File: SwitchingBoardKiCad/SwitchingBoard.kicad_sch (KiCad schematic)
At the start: 45 parts

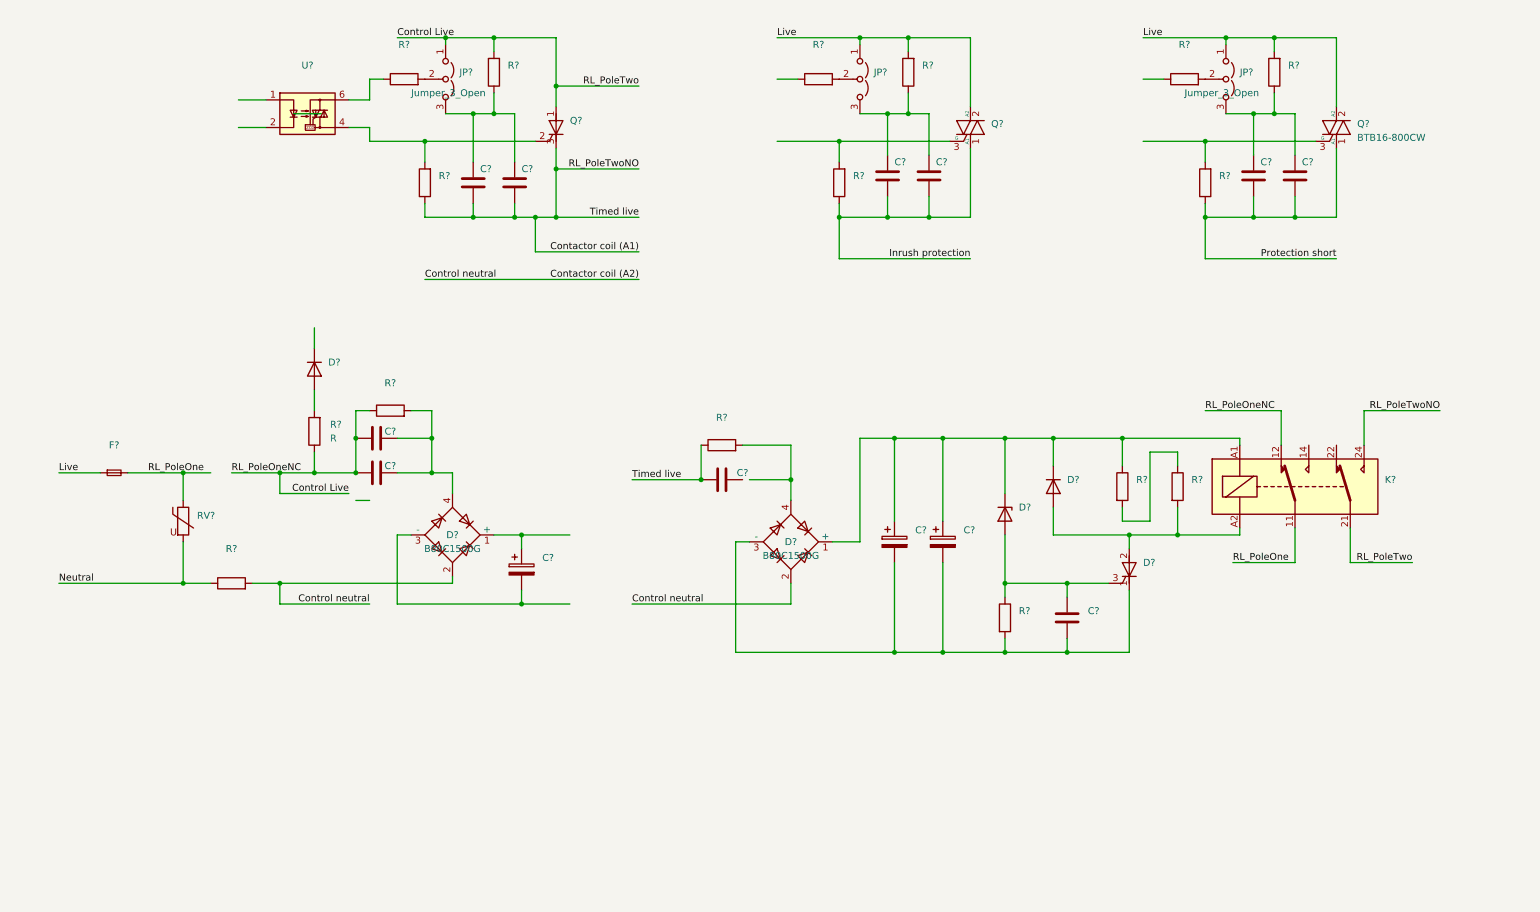
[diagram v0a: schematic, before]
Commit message: KiCad switching board schematic passes initial ERC.
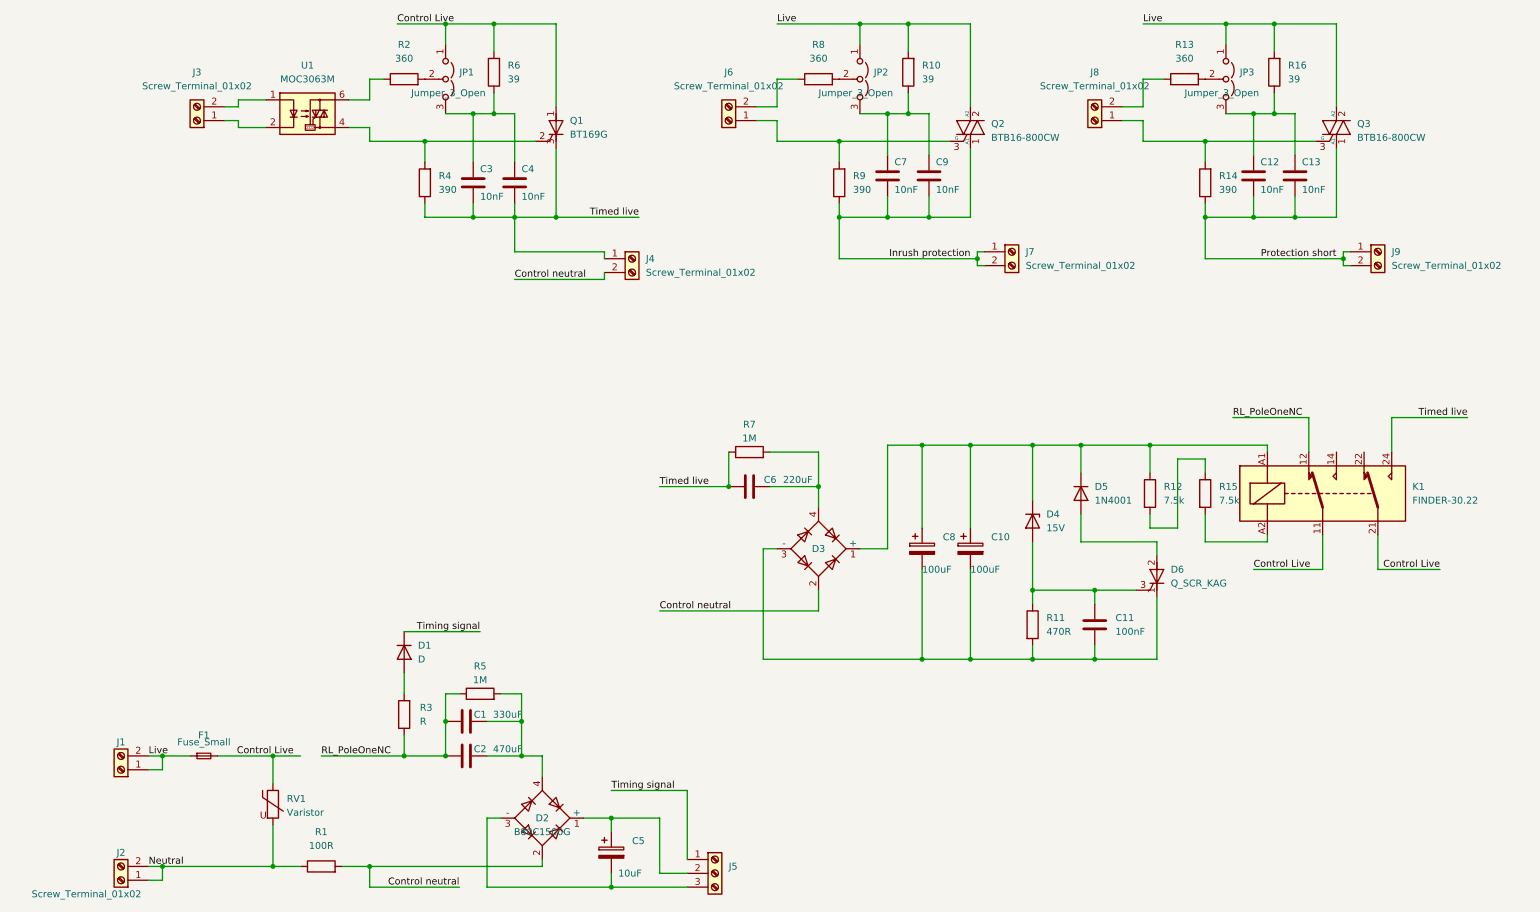
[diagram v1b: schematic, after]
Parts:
- added J1: (no value), symbol Connector:Screw_Terminal_01x02
- added J2, J3, J4, J6, J7, J8, J9: Screw_Terminal_01x02, symbol Connector:Screw_Terminal_01x02
- added J5: (no value), symbol Connector:Screw_Terminal_01x03
- C1: renamed from C?; value (none) -> 330uF
- C10, C8: renamed from C?; value (none) -> 100uF
- C11: renamed from C?; value (none) -> 100nF
- C12, C13, C3, C4, C7, C9: renamed from C?; value (none) -> 10nF
- C2: renamed from C?; value (none) -> 470uF
- C5: renamed from C?; value (none) -> 10uF
- C6: renamed from C?; value (none) -> 220uF
- D1: renamed from D?; value (none) -> D; footprint (none) -> Diode_SMD:D_SMB
- D3: renamed from D?; value B80C1500G -> (none); footprint Diode_THT:Diode_Bridge_Round_D9.8mm -> (none)
- D4: renamed from D?; value (none) -> 15V
- D5: renamed from D?; value (none) -> 1N4001; footprint (none) -> Diode_THT:D_DO-41_SOD81_P10.16mm_Horizontal
- D6: renamed from D?; value (none) -> Q_SCR_KAG
- F1: renamed from F?; value (none) -> Fuse_Small; footprint (none) -> Connector_Coaxial:SMB_Jack_Vertical
- JP2: renamed from JP?; value (none) -> Jumper_3_Open
- K1: renamed from K?; value (none) -> FINDER-30.22; footprint (none) -> Relay_THT:Relay_DPDT_Finder_40.52
- Q1: renamed from Q?; value (none) -> BT169G; footprint (none) -> Package_TO_SOT_THT:TO-92_Inline
- Q2: renamed from Q?; value (none) -> BTB16-800CW; footprint (none) -> Package_TO_SOT_THT:TO-220-3_Vertical
- R1: renamed from R?; value (none) -> 100R
- R10, R16, R6: renamed from R?; value (none) -> 39
- R11: renamed from R?; value (none) -> 470R
- R12, R15: renamed from R?; value (none) -> 7.5k
- R13, R2, R8: renamed from R?; value (none) -> 360
- R14, R4, R9: renamed from R?; value (none) -> 390
- R5, R7: renamed from R?; value (none) -> 1M
- RV1: renamed from RV?; value (none) -> Varistor
- U1: renamed from U?; value (none) -> MOC3063M
- gave numbers to parts that had none: 5
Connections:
- net RL_PoleOne is gone; now on net Control Live: F1.2, K1.11, RV1.1
- net Control Live: no longer C1.1, C2.1, K1.12, R3.1, R5.1
- net Inrush protection: now also J7.1 (Pin_1), J7.2 (Pin_2)
- net Live: now also J1.1 (Pin_1), J1.2 (Pin_2)
- net Neutral: now also J2.1 (Pin_1), J2.2 (Pin_2)
- net Protection short: now also J9.1 (Pin_1), J9.2 (Pin_2)
- net at D5.2 (A), D6.2 (A): no longer K1.A2, R15.2
- net at Q2.3 (G), R9.2: now also J6.1 (Pin_1)
- net at D3.4, R7.2: now also C6.2
- net at Q3.3 (G), R14.2: now also J8.1 (Pin_1)
- net at U1.1: now also J3.2 (Pin_2)
- net at U1.2: now also J3.1 (Pin_1)
- net Timing signal: now reaches D1.1 (K)
- net Timing signal: now also J5.1 (Pin_1)
- net at R8.1: now also J6.2 (Pin_2)
- net at C5.1, D2.1 (+): now also J5.2 (Pin_2)
- net at C5.2, D2.3 (-): now also J5.3 (Pin_3)
- net at R13.1: now also J8.2 (Pin_2)
- net Contactor coil (A1) renamed Timed live
- net Timed live: now also J4.1 (Pin_1)
- net Contactor coil (A2) renamed Control neutral
- net Control neutral: now also J4.2 (Pin_2)
- new net: K1.A2, R15.2
- new net RL_PoleOneNC: C1.1, C2.1, K1.12, R3.1, R5.1
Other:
- moved on the sheet: C1, C10, C11, C2, C5, C6, C8, D1, D2, D3, D4, D5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

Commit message: Assigned footprints
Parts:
- removed F1: Fuse_Small, Connector_Coaxial:SMB_Jack_Vertical, symbol Device:Fuse_Small
- added J10, J11: (no value), symbol Connector:Screw_Terminal_01x02
- D1: value D -> (none); footprint Diode_SMD:D_SMB -> (none)
- R3: value R -> (none)
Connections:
- net Control Live: now also J11.1 (Pin_1), J11.2 (Pin_2)
- net Live: now also J10.1 (Pin_1), J10.2 (Pin_2)

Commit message: Initial grouping of components on PCB
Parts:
- C1: footprint (none) -> Capacitor_THT:C_Rect_L18.0mm_W9.0mm_P15.00mm_FKS3_FKP3
- C10, C8: footprint (none) -> Capacitor_THT:CP_Radial_D6.3mm_P2.50mm
- C11: footprint (none) -> Capacitor_THT:C_Disc_D5.0mm_W2.5mm_P5.00mm
- C12, C13, C3, C4, C7, C9: footprint (none) -> Capacitor_THT:C_Rect_L18.0mm_W5.0mm_P15.00mm_FKS3_FKP3
- C2: footprint (none) -> Capacitor_THT:C_Rect_L26.5mm_W10.5mm_P22.50mm_MKS4
- C5: footprint (none) -> Capacitor_THT:CP_Radial_D5.0mm_P2.00mm
- C6: footprint (none) -> Capacitor_THT:C_Rect_L26.5mm_W6.0mm_P22.50mm_MKS4
- D1: value (none) -> STTH110; footprint (none) -> Diode_THT:D_DO-41_SOD81_P10.16mm_Horizontal
- D3: value (none) -> B80C800G; footprint (none) -> Diode_THT:Diode_Bridge_Round_D9.8mm
- D4: footprint (none) -> Diode_THT:D_DO-35_SOD27_P7.62mm_Horizontal
- D6: footprint (none) -> Package_TO_SOT_THT:TO-220-3_Horizontal_TabDown
- J1: value (none) -> Screw_Terminal_01x02; footprint (none) -> TerminalBlock:TerminalBlock_Altech_AK300-2_P5.00mm
- J2, J3, J4, J6, J7, J8, J9: footprint (none) -> TerminalBlock:TerminalBlock_Altech_AK300-2_P5.00mm
- J5: value (none) -> Screw_Terminal_01x03; footprint (none) -> TerminalBlock:TerminalBlock_Altech_AK300-3_P5.00mm
- JP1, JP2, JP3: footprint (none) -> TerminalBlock:TerminalBlock_bornier-3_P5.08mm
- R1, R5, R7: footprint (none) -> Resistor_THT:R_Axial_Power_L20.0mm_W6.4mm_P22.40mm
- R10, R11, R12, R13, R14, R15, R16, R2, R4, R6, R8, R9: footprint (none) -> Resistor_THT:R_Axial_DIN0207_L6.3mm_D2.5mm_P10.16mm_Horizontal
- R3: value (none) -> 1M; footprint (none) -> Resistor_THT:R_Axial_Power_L20.0mm_W6.4mm_P22.40mm
- RV1: footprint (none) -> Varistor:RV_Disc_D12mm_W4.3mm_P7.5mm
- U1: footprint (none) -> Package_DIP:DIP-6_W7.62mm_LongPads
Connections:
- net at D5.2 (A), D6.2 (A): now also K1.A2, R15.2

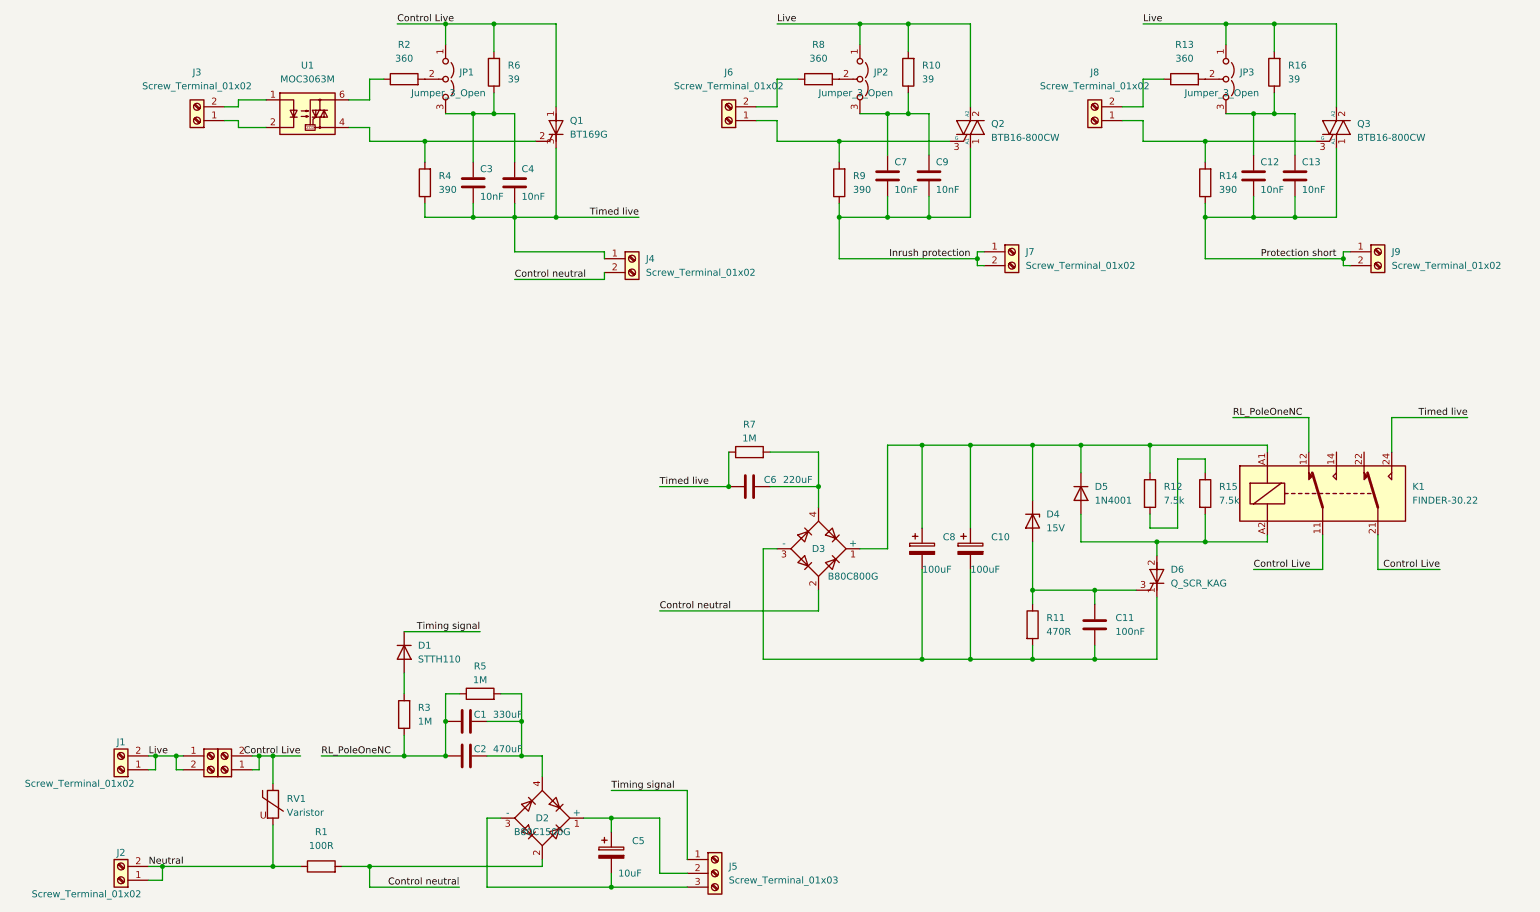
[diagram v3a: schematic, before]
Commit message: Removed optocoupler from this board and updated the fuseholder footprint.
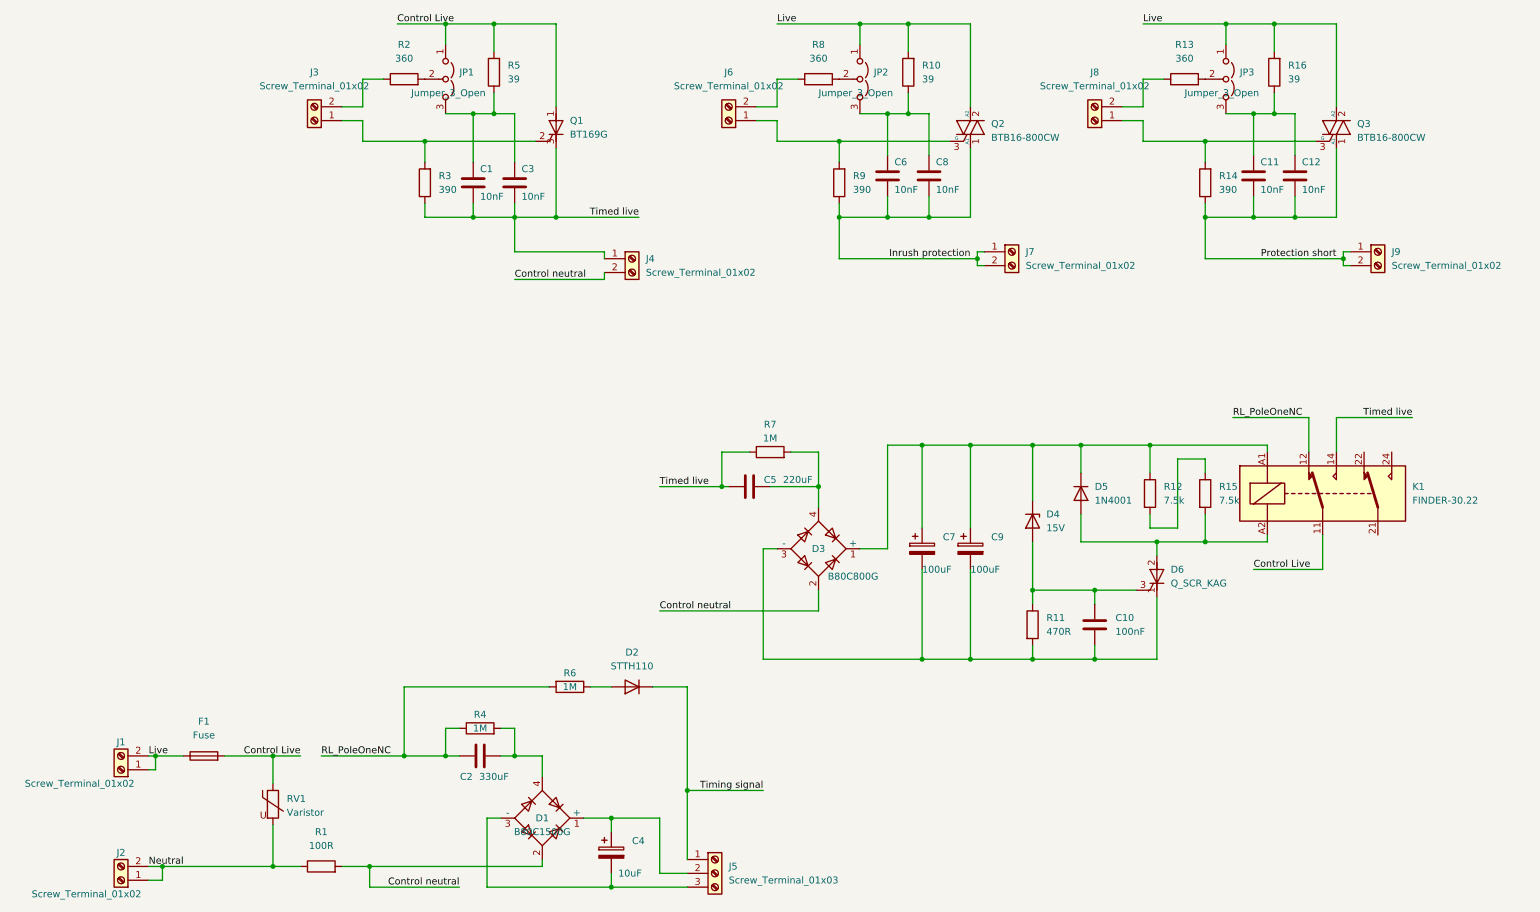
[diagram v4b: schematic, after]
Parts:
- removed C2: 470uF, Capacitor_THT:C_Rect_L26.5mm_W10.5mm_P22.50mm_MKS4, symbol Device:C
- removed J10, J11: (no value), symbol Connector:Screw_Terminal_01x02
- removed U1: MOC3063M, Package_DIP:DIP-6_W7.62mm_LongPads, symbol Relay_SolidState:MOC3063M
- added F1: Fuse, FuseHolders:Fuseholder_Clip-5x20mm&6.3x32_Schurter_OG_Lateral_P20.00x5.00mm_D1.3mm_Horizontal, symbol Device:Fuse
- renumbered C3 to C1, C11 to C10, C12 to C11, C13 to C12, C1 to C2, C4 to C3, C5 to C4, C6 to C5, C7 to C6, C8 to C7, C9 to C8, C10 to C9, D2 to D1, D1 to D2, R4 to R3, R5 to R4, R6 to R5, R3 to R6
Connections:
- net Control Live: now also F1.2; no longer K1.21
- net Live: now also F1.1
- net RL_PoleOneNC: now also R6.2; no longer R6.1
- net Timed live: now also K1.14; no longer K1.24
- net at Q1.2 (G), R3.2: now also J3.1 (Pin_1)
- net at J3.2 (Pin_2): now also R2.1
- net at D2.2 (A): now also R6.1; no longer R6.2
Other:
- moved on the sheet: C2, D2, J3, R4, R6, R7

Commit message: Added custom fuse footprint and updated PCB.
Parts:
- F1: footprint FuseHolders:Fuseholder_Clip-5x20mm&6.3x32_Schurter_OG_Lateral_P20.00x5.00mm_D1.3mm_Horizontal -> (none)
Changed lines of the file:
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@@
     (property "Reference" "F1" (id 0) (at 48.26 158.75 90))
     (property "Value" "Fuse" (id 1) (at 48.26 161.29 90))
-    (property "Footprint" "FuseHolders:Fuseholder_Clip-5x20mm&6.3x32_Schurter_OG_Lateral_P20.00x5.00mm_D1.3mm_Horizontal" (id 2) (at 48.26 166.878 90)
+    (property "Footprint" "" (id 2) (at 48.26 166.878 90)
       (effects (font (size 1.27 1.27)) hide)
     )
@@
     )
     (path "/95f38c41-d1ce-487a-b870-eb7296f9e1b5"
-      (reference "F1") (unit 1) (value "Fuse") (footprint "FuseHolders:Fuseholder_Clip-5x20mm&6.3x32_Schurter_OG_Lateral_P20.00x5.00mm_D1.3mm_Horizontal")
+      (reference "F1") (unit 1) (value "Fuse") (footprint "ITFootprints:Fuseholder_Clip-5x20mmOr6.3x32_Schurter_OG_Lateral_P20.00x5.00mm_D1.3mm_Horizontal")
     )
     (path "/9ec871c1-4e05-4164-b89f-2e9855186b95"

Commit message: Playing with layout and routing in KiCad
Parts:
- added D3: D_TVS_Filled, Diode_THT:D_DO-15_P12.70mm_Horizontal, symbol Device:D_TVS_Filled
- F1: footprint (none) -> ITFootprints:Fuseholder_Clip-5x20mmOr6.3x32_Schurter_OG_Lateral_P20.00x5.00mm_D1.3mm_Horizontal
- JP1, JP2, JP3: footprint TerminalBlock:TerminalBlock_bornier-3_P5.08mm -> TerminalBlock_4Ucon:TerminalBlock_4Ucon_1x03_P3.50mm_Horizontal
- R10, R16, R5: value 39 -> 47
- renumbered D3 to D4, D4 to D5, D5 to D6, D6 to D7, J6 to J5, J5 to J6
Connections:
- net at Q3.3 (G), R14.2: now also J8.2 (Pin_2); no longer J8.1 (Pin_1)
- net at R13.1: now also J8.1 (Pin_1); no longer J8.2 (Pin_2)
- net at C4.1, D1.1 (+), J6.2 (Pin_2): now also D3.2 (A2)
- net at C4.2, D1.3 (-), J6.3 (Pin_3): now also D3.1 (A1)
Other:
- moved on the sheet: J6, J8
